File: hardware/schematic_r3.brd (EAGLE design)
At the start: 53.3 x 45.7 mm, 87 parts, among them Q1 SI2333DDS-T1-GE3CT-ND, U1 STM32L052K8, U2 BME280, U3 ADXL345, U4 HX1, U5 TPS62160, U6 TPS62160, U7 COPERNICUSSMD, U8 LMP7702, Y1 32.768kHz

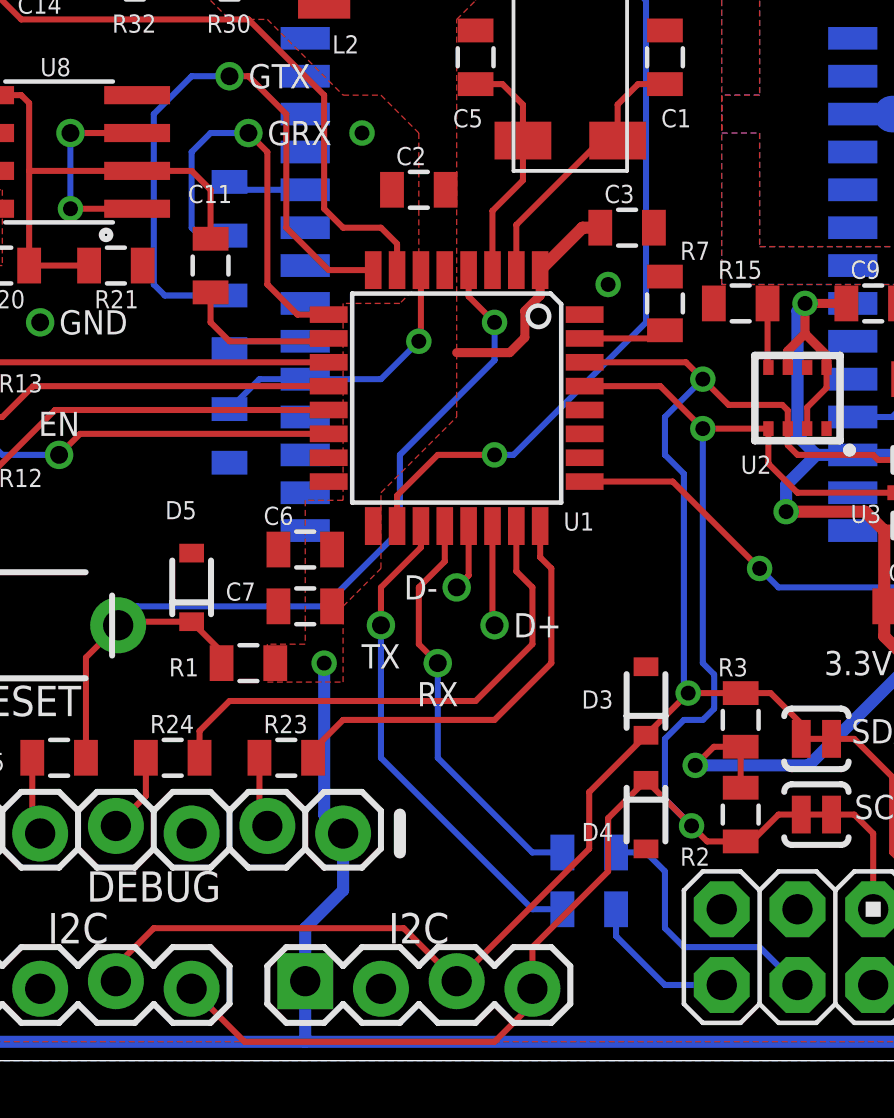
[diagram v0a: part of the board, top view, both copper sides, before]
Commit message: Update r3 schematics and board to fix minor issues
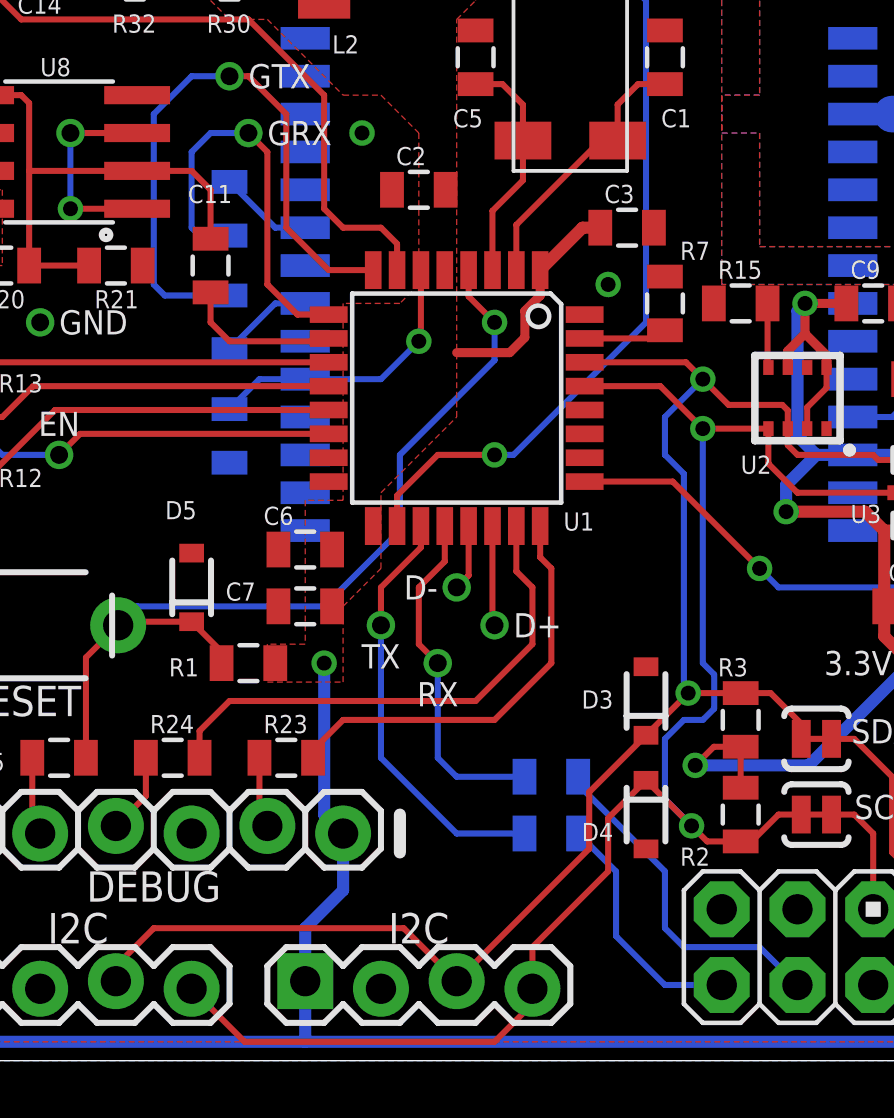
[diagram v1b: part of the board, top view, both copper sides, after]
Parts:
- moved R10 2.84 mm to (34.9, 7.62)
- moved R9 2.84 mm to (34.9, 9.53)
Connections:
- net RX_GPS: now also U7.21; no longer U7.20
- net TX_GPS: now also U7.23; no longer U7.24
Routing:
- net RX_PI: track 5.12 -> 8.19 mm
- net TX_PI: track 9.04 -> 11.5 mm
- net U1TX: track 16.5 -> 14.2 mm
- net U1RX: track 13.9 -> 11.6 mm
- net TX_GPS: track 2.65 -> 3.55 mm
- net RX_GPS: track 2.65 -> 3.55 mm
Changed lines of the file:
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@@
 <attribute name="VALUE" x="14.478" y="21.336" size="0.4064" layer="27" rot="R270" align="center"/>
 </element>
-<element name="R9" library="SparkFun-Passives" package="0805" value="100" x="36.195" y="6.985" smashed="yes" rot="MR180">
-<attribute name="NAME" x="33.528" y="7.4295" size="0.6096" layer="26" rot="MR180"/>
-<attribute name="VALUE" x="36.068" y="7.239" size="0.4064" layer="28" rot="MR90" align="center"/>
-</element>
-<element name="R10" library="SparkFun-Passives" package="0805" value="100" x="36.195" y="5.08" smashed="yes" rot="MR180">
-<attribute name="NAME" x="32.893" y="5.5245" size="0.6096" layer="26" rot="MR180"/>
-<attribute name="VALUE" x="36.068" y="5.334" size="0.4064" layer="28" rot="MR90" align="center"/>
+<element name="R9" library="SparkFun-Passives" package="0805" value="100" x="34.925" y="9.525" smashed="yes" rot="MR180">
+<attribute name="NAME" x="32.258" y="9.9695" size="0.6096" layer="26" rot="MR180"/>
+<attribute name="VALUE" x="34.798" y="9.779" size="0.4064" layer="28" rot="MR90" align="center"/>
+</element>
+<element name="R10" library="SparkFun-Passives" package="0805" value="100" x="34.925" y="7.62" smashed="yes" rot="MR180">
+<attribute name="NAME" x="31.623" y="8.0645" size="0.6096" layer="26" rot="MR180"/>
+<attribute name="VALUE" x="34.798" y="7.874" size="0.4064" layer="28" rot="MR90" align="center"/>
 </element>
 <element name="R11" library="SparkFun-Passives" package="0805" value="10K" x="5.08" y="29.21" smashed="yes" rot="R270">
@@
 <via x="31.115" y="13.335" extent="1-16" drill="0.6"/>
 <wire x1="31.115" y1="13.335" x2="31.115" y2="10.16" width="0.2032" layer="16"/>
-<wire x1="31.115" y1="10.16" x2="34.29" y2="6.985" width="0.2032" layer="16"/>
-<wire x1="34.29" y1="6.985" x2="35.295" y2="6.985" width="0.2032" layer="16"/>
+<wire x1="34.025" y1="9.525" x2="31.75" y2="9.525" width="0.2032" layer="16"/>
+<wire x1="31.75" y1="9.525" x2="31.115" y2="10.16" width="0.2032" layer="16"/>
 </signal>
 <signal name="U1TX">
@@
 <via x="29.21" y="14.605" extent="1-16" drill="0.6"/>
 <wire x1="29.21" y1="14.605" x2="29.21" y2="10.16" width="0.2032" layer="16"/>
-<wire x1="29.21" y1="10.16" x2="34.29" y2="5.08" width="0.2032" layer="16"/>
-<wire x1="34.29" y1="5.08" x2="35.295" y2="5.08" width="0.2032" layer="16"/>
 <wire x1="30.55" y1="17.9324" x2="30.55" y2="17.215" width="0.2032" layer="1"/>
 <wire x1="30.55" y1="17.215" x2="29.21" y2="15.875" width="0.2032" layer="1"/>
 <wire x1="29.21" y1="14.605" x2="29.21" y2="15.875" width="0.2032" layer="1"/>
+<wire x1="34.025" y1="7.62" x2="31.75" y2="7.62" width="0.2032" layer="16"/>
+<wire x1="31.75" y1="7.62" x2="29.21" y2="10.16" width="0.2032" layer="16"/>
 </signal>
 <signal name="PPS">
@@
 <wire x1="41.91" y1="3.81" x2="39.37" y2="3.81" width="0.2032" layer="16"/>
 <wire x1="39.37" y1="3.81" x2="38.735" y2="4.445" width="0.2032" layer="16"/>
-<wire x1="37.095" y1="6.985" x2="38.1" y2="6.985" width="0.2032" layer="16"/>
-<wire x1="38.1" y1="6.985" x2="38.735" y2="6.35" width="0.2032" layer="16"/>
 <wire x1="38.735" y1="6.35" x2="38.735" y2="4.445" width="0.2032" layer="16"/>
+<wire x1="38.735" y1="6.35" x2="35.825" y2="9.26" width="0.2032" layer="16"/>
+<wire x1="35.825" y1="9.525" x2="35.825" y2="9.26" width="0.2032" layer="16"/>
 </signal>
 <signal name="RX_PI">
@@
 <wire x1="40.64" y1="2.54" x2="38.735" y2="2.54" width="0.2032" layer="16"/>
 <wire x1="38.735" y1="2.54" x2="37.095" y2="4.18" width="0.2032" layer="16"/>
-<wire x1="37.095" y1="5.08" x2="37.095" y2="4.18" width="0.2032" layer="16"/>
+<wire x1="37.095" y1="4.18" x2="37.095" y2="6.35" width="0.2032" layer="16"/>
+<wire x1="37.095" y1="6.35" x2="35.825" y2="7.62" width="0.2032" layer="16"/>
 </signal>
 <signal name="+9V">
@@
 <signal name="TX_GPS">
 <contactref element="R5" pad="2"/>
-<contactref element="U7" pad="24"/>
-<wire x1="26.67" y1="29.21" x2="24.395" y2="29.21" width="0.2032" layer="16"/>
 <wire x1="24.395" y1="29.21" x2="24.13" y2="29.475" width="0.2032" layer="16"/>
+<contactref element="U7" pad="23"/>
+<wire x1="26.67" y1="27.94" x2="25.665" y2="27.94" width="0.2032" layer="16"/>
+<wire x1="25.665" y1="27.94" x2="24.13" y2="29.475" width="0.2032" layer="16"/>
 </signal>
 <signal name="RX_GPS">
 <contactref element="R6" pad="2"/>
-<contactref element="U7" pad="20"/>
-<wire x1="26.67" y1="24.13" x2="24.395" y2="24.13" width="0.2032" layer="16"/>
 <wire x1="24.395" y1="24.13" x2="24.13" y2="23.865" width="0.2032" layer="16"/>
+<contactref element="U7" pad="21"/>
+<wire x1="26.67" y1="25.4" x2="25.665" y2="25.4" width="0.2032" layer="16"/>
+<wire x1="25.665" y1="25.4" x2="24.13" y2="23.865" width="0.2032" layer="16"/>
 </signal>
 <signal name="RFIN">
